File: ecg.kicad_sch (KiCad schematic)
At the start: 21 parts, among them SW1 SW_Push, SW2 SW_Push, U1 ESP32-S3-PICO-1-N8R2, Y1 Crystal

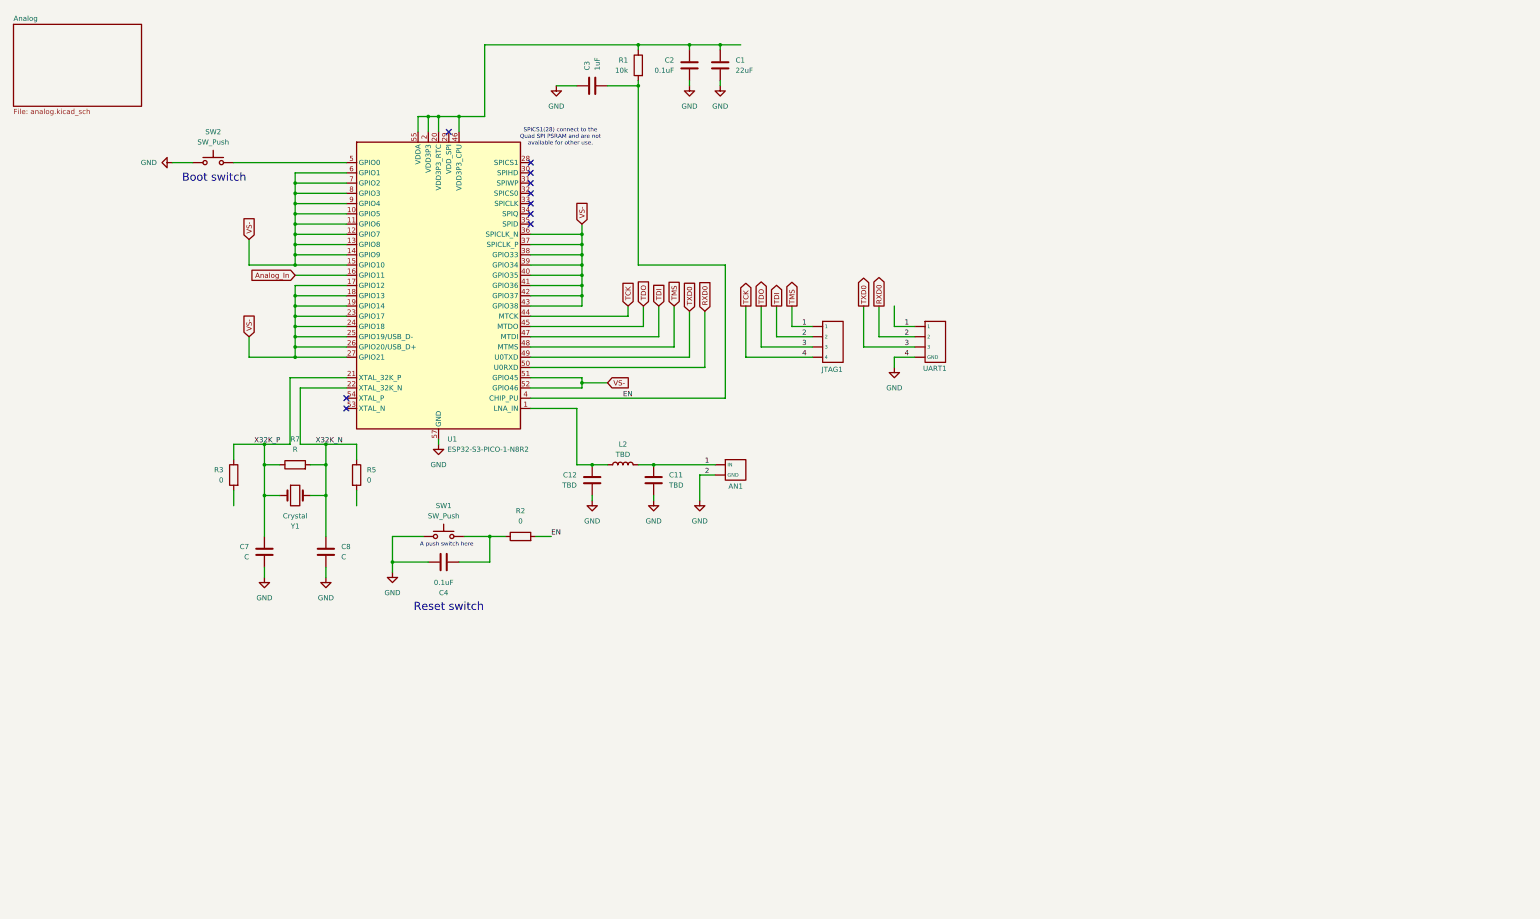
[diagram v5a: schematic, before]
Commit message: Remove external oscillator, connect all GND to VS-, Fix ERC Errors.
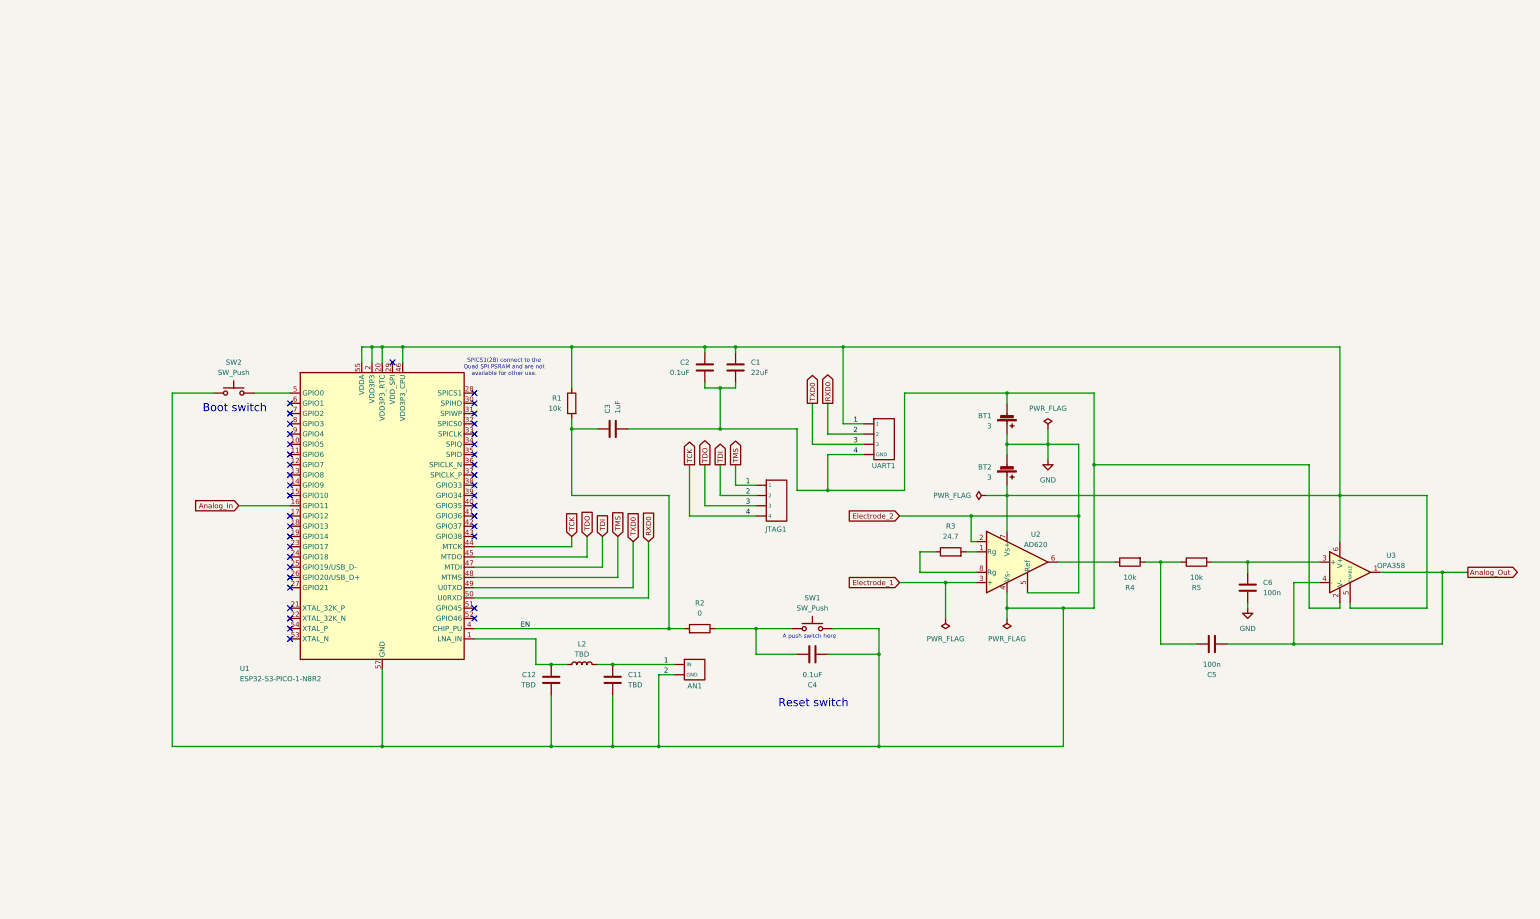
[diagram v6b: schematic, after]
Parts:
- removed C7, C8: C, Capacitor_SMD:C_0201_0603Metric, symbol Device:C
- removed R7: R, Resistor_SMD:R_0201_0603Metric, symbol Device:R
- removed Y1: Crystal, symbol Device:Crystal
- added BT1, BT2: 3, symbol Device:Battery_Cell
- added C5, C6: 100n, Capacitor_SMD:C_0201_0603Metric, symbol Device:C
- added R4: 10k, Resistor_SMD:R_0201_0603Metric, symbol Device:R
- added U2: AD620, ad620:R_8_ADI-M, symbol Amplifier_Instrumentation:AD620
- added U3: OPA358, opa358:DCK6-M, symbol OPA358:OPA358
- R3: value 0 -> 24.7
- R5: value 0 -> 10k
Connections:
- net EN: now also C3.2; no longer C3.1
- net GND: now also BT1.1 (+), BT2.2 (-), C6.2, U2.2 (-), U2.5 (Ref); no longer AN1. (IN), C1.1, C11.2, C12.2, C2.1, C3.2, C4.1, JTAG1. (4), SW1.1, SW2.1, U1.44 (MTCK), U1.47 (MTDI), U1.50 (U0RXD), U1.57 (GND), UART1. (GND)
- net TMS: now also C1.2, C2.2, R1.1, U1.2 (VDD3P3), U1.20 (VDD3P3_RTC), U1.3 (VDD3P3), U1.46 (VDD3P3_CPU), U1.55 (VDDA), U1.56 (VDDA), BT2.1 (+), U2.7 (Vs+), U3.5 (ENABLE), U3.6 (V+)
- net at R3.2: now also U2.1 (Rg)
- net at R5.2: now also C6.1, U3.3 (+)
- removed net VS-: U1.10 (GPIO5), U1.11 (GPIO6), U1.12 (GPIO7), U1.13 (GPIO8), U1.14 (GPIO9), U1.15 (GPIO10), U1.17 (GPIO12), U1.18 (GPIO13), U1.19 (GPIO14), U1.23 (GPIO17), U1.24 (GPIO18), U1.25 (GPIO19/USB_D-), U1.26 (GPIO20/USB_D+), U1.27 (GPIO21), U1.36 (SPICLK_N), U1.37 (SPICLK_P), U1.38 (GPIO33), U1.39 (GPIO34), U1.40 (GPIO35), U1.41 (GPIO36), U1.42 (GPIO37), U1.43 (GPIO38), U1.51 (GPIO45), U1.52 (GPIO46), U1.6 (GPIO1), U1.7 (GPIO2), U1.8 (GPIO3), U1.9 (GPIO4)
- net X32K_N: no longer names the net of R5.1
- net X32K_N: now also C5.1, R4.2; no longer U1.22 (XTAL_32K_N)
- net X32K_P: no longer names the net of R3.1
- net X32K_P: now also U2.8 (Rg); no longer U1.21 (XTAL_32K_P)
- new net: R4.1, U2.6
- new net Analog_Out: C5.2, U3.1, U3.4 (-)
- new net Electrode_1: U2.3 (+)
- new net RXD0: AN1. (IN), BT1.2 (-), C1.1, C11.2, C12.2, C2.1, C3.1, C4.1, JTAG1. (4), SW1.1, SW2.1, U1.44 (MTCK), U1.47 (MTDI), U1.50 (U0RXD), U1.57 (GND), U2.4 (Vs-), U3.2 (V-), UART1. (GND)
- no-connect marks 10 -> 40
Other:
- removed sheet Analog
- moved on the sheet: AN1, C1, C11, C12, C2, C3, C4, L2, R1, R2, SW1, SW2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

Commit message: LDO, UART, USB
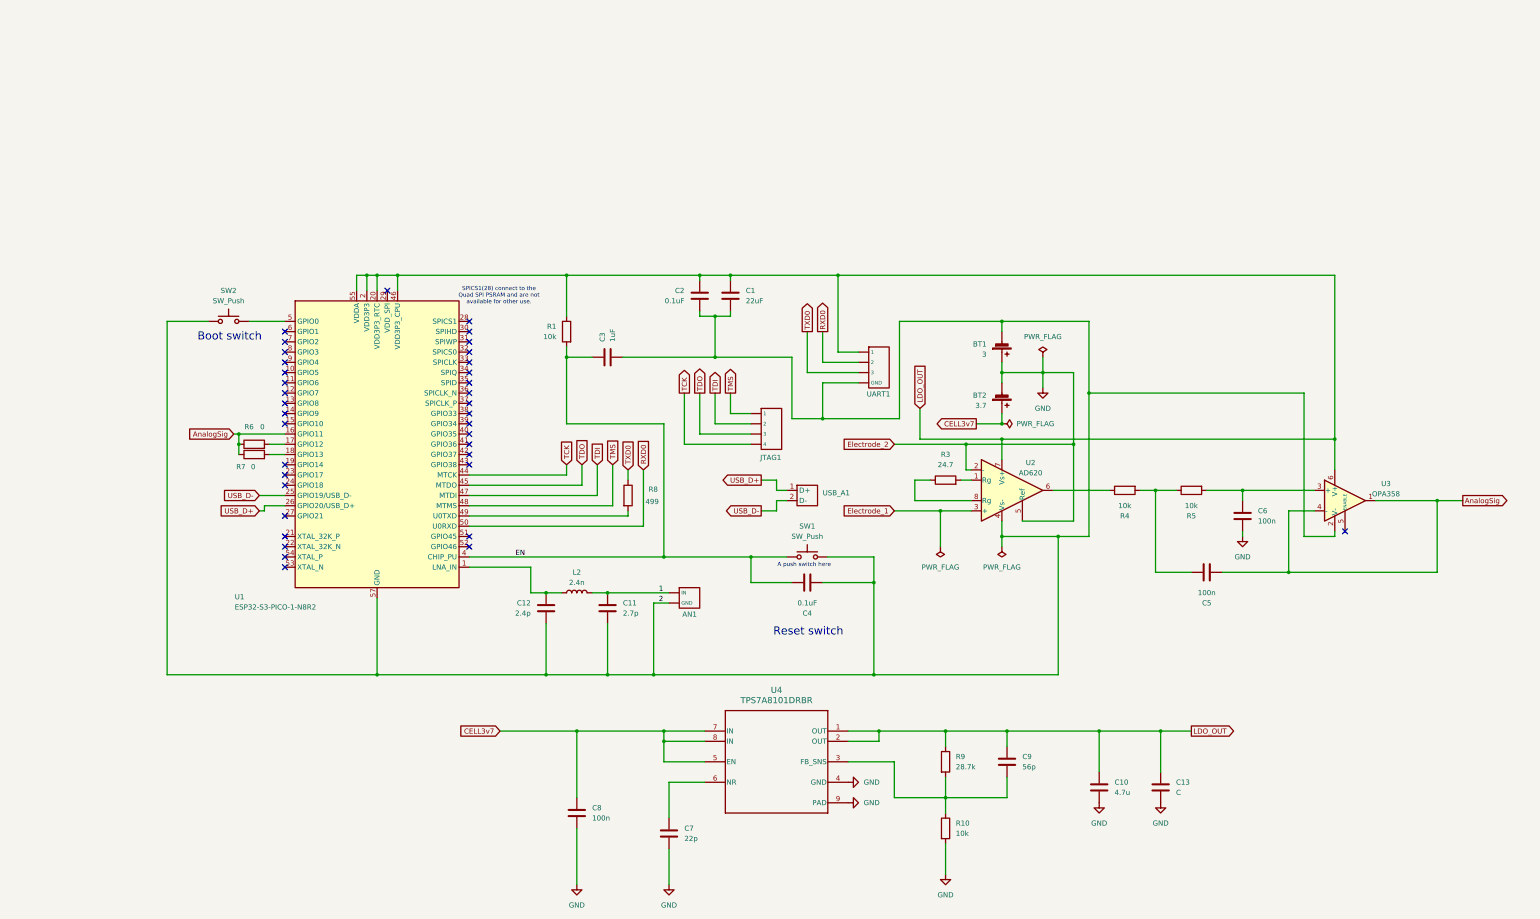
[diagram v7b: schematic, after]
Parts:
- removed R2: 0, Resistor_SMD:R_0201_0603Metric, symbol Device:R
- added C10: 4.7u, symbol Device:C
- added C13: C, symbol Device:C
- added C7: 22p, symbol Device:C
- added C8: 100n, symbol Device:C
- added C9: 56p, symbol Device:C
- added R10: 10k, symbol Device:R
- added R6, R7: 0, symbol Device:R
- added R8: 499, symbol Device:R
- added R9: 28.7k, symbol Device:R
- added U4: TPS7A8101DRBR, DRB0008A, symbol TPS7A8101DRBR:TPS7A8101DRBR
- added USB_A1: ~, symbol usb_a:USB_A
- BT2: value 3 -> 3.7
- C11: value TBD -> 2.7p
- C12: value TBD -> 2.4p
- L2: value TBD -> 2.4n
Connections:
- net Analog_Out is gone; now on net AnalogSig: C5.2, U3.1, U3.4 (-)
- net EN: now also C4.2, SW1.2
- net GND: now also C10.2, C13.2, C7.2, C8.2, R10.2, U4.4 (GND), U4.9 (PAD)
- net RXD0: no longer AN1. (IN), BT1.2 (-), C1.1, C11.2, C12.2, C2.1, C3.1, C4.1, JTAG1. (4), SW1.1, SW2.1, U1.44 (MTCK), U1.47 (MTDI), U1.57 (GND), U2.4 (Vs-), U3.2 (V-)
- net TDO: no longer U1.49 (U0TXD), UART1. (GND)
- net TMS: no longer AN1. (IN), BT2.1 (+), C1.2, C11.1, C2.2, L2.2, R1.1, U1.2 (VDD3P3), U1.20 (VDD3P3_RTC), U1.3 (VDD3P3), U1.46 (VDD3P3_CPU), U1.55 (VDDA), U1.56 (VDDA), U2.7 (Vs+), U3.5 (ENABLE), U3.6 (V+), UART1. (GND)
- net at U1.17 (GPIO12): now also R6.2
- net at U1.18 (GPIO13): now also R7.2
- net USB_D-: now reaches U1.25 (GPIO19/USB_D-)
- net USB_D-: now also USB_A1.2 (D-)
- net USB_D+: now reaches U1.26 (GPIO20/USB_D+)
- net USB_D+: now also USB_A1.1 (D+)
- net Analog_In renamed AnalogSig
- net AnalogSig: now also R6.1, R7.1
- new net: C9.2, R10.1, R9.2, U4.3 (FB_SNS)
- new net: C7.1, U4.6 (NR)
- new net: R8.2, U1.49 (U0TXD)
- new net 1: AN1. (IN), C11.1, L2.2
- new net 2: AN1. (IN), BT1.2 (-), C1.1, C11.2, C12.2, C2.1, C3.1, C4.1, SW1.1, SW2.1, U1.57 (GND), U2.4 (Vs-), U3.2 (V-), UART1. (GND)
- new net CELL3v7: BT2.1 (+), C8.1, U4.5 (EN), U4.7 (IN), U4.8 (IN)
- new net LDO_OUT: C1.2, C10.1, C13.1, C2.2, C9.1, R1.1, R9.1, U1.2 (VDD3P3), U1.20 (VDD3P3_RTC), U1.3 (VDD3P3), U1.46 (VDD3P3_CPU), U1.55 (VDDA), U1.56 (VDDA), U2.7 (Vs+), U3.6 (V+), U4.1 (OUT), U4.2 (OUT), UART1. (GND)
- new net TCK: JTAG1. (4), U1.44 (MTCK)
- new net TDI: JTAG1. (4), U1.47 (MTDI)
- new net TXD0: R8.1, UART1. (GND)
- no-connect marks 40 -> 37
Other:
- moved on the sheet: AN1, BT1, BT2, C1, C11, C12, C2, C3, C4, C5, C6, JTAG1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
